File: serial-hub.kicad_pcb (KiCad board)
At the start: 2 copper layers, 100 x 100 mm, 55 parts, among them J1 USB_C_Receptacle_USB2.0, J2 RJ45_LED_Shielded, J3 RJ45_LED_Shielded, J4 RJ45_LED_Shielded, J5 RJ45_LED_Shielded, U1 CH344, U2 AMS1117-3.3, U3 MAX232, U4 MAX232, U5 MAX232, U6 MAX232, Y1 8MHz

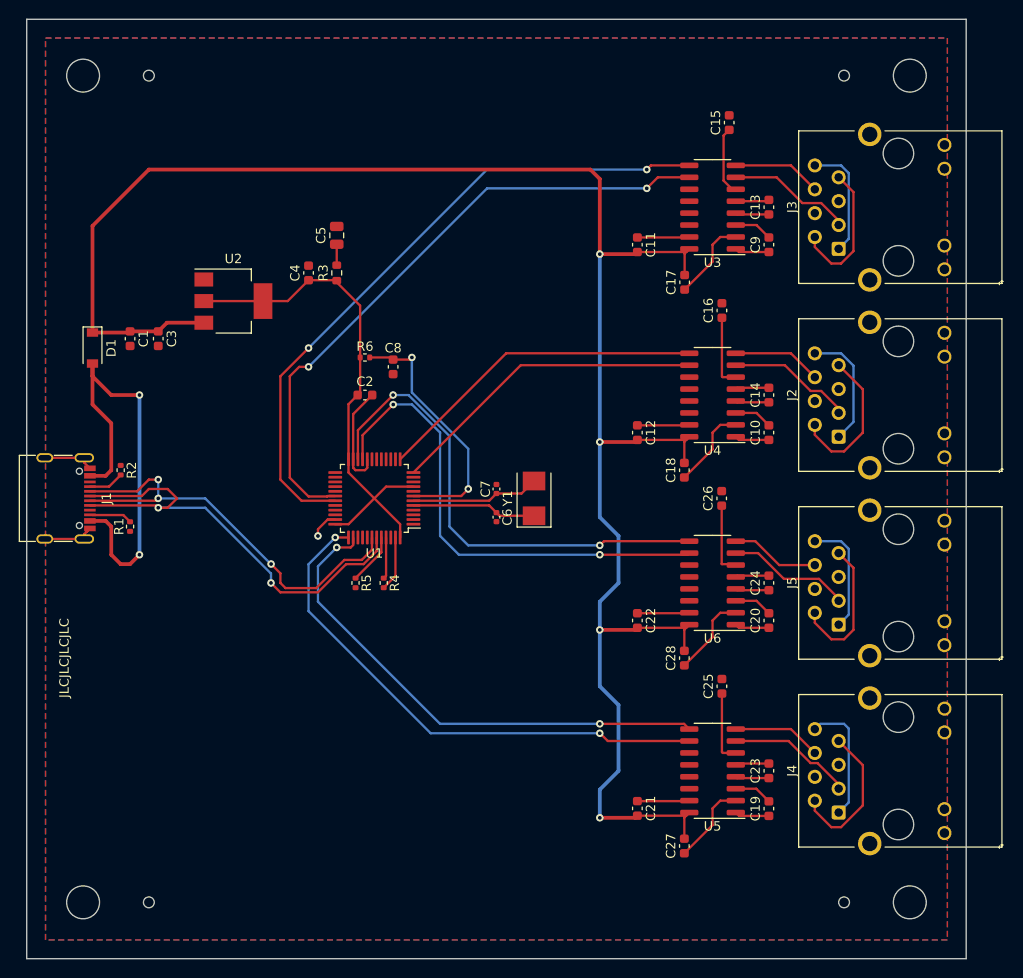
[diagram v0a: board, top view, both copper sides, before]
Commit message: add test-pins for UART
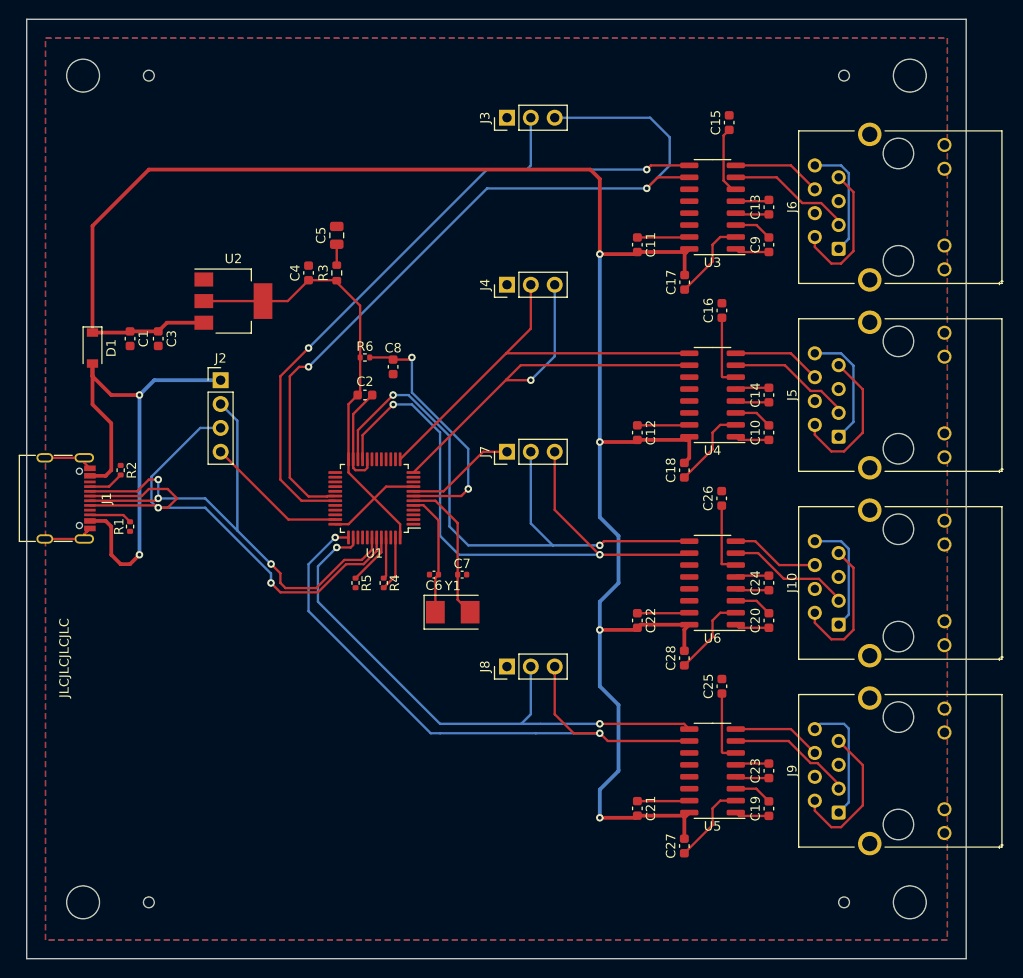
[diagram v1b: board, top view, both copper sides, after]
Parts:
- added J2: Conn_01x04_Male, Connector_PinHeader_2.54mm:PinHeader_1x04_P2.54mm_Vertical, F.Cu at (40.6, 58.4)
- added J3: Conn_01x03_Male, Connector_PinHeader_2.54mm:PinHeader_1x03_P2.54mm_Vertical, F.Cu at (71.1, 30.5)
- added J4: Conn_01x03_Male, Connector_PinHeader_2.54mm:PinHeader_1x03_P2.54mm_Vertical, F.Cu at (71.1, 48.3)
- added J7: Conn_01x03_Male, Connector_PinHeader_2.54mm:PinHeader_1x03_P2.54mm_Vertical, F.Cu at (71.1, 66.0)
- added J8: Conn_01x03_Male, Connector_PinHeader_2.54mm:PinHeader_1x03_P2.54mm_Vertical, F.Cu at (71.1, 88.9)
- moved Y1 14.9 mm to (65.3, 83.1), turned to 0 degrees
- moved C7 9.82 mm to (66.3, 79.1), turned to 0 degrees
- moved C6 9.03 mm to (63.4, 79.1), turned to 180 degrees
- renumbered J5 to J10, J2 to J5, J3 to J6, J4 to J9
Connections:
- net Net-(D1-Pad2) renamed VCC
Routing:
- net GND: track 53.9 -> 77.8 mm, vias 1 -> 0
- net /C0_TX: track 67.8 -> 87.3 mm
- net /HOST_DM: track 47.5 -> 61.7 mm
- net /C1_TX: track 34.1 -> 47.9 mm, vias 0 -> 1
- net /HOST_DP: track 50.6 -> 63.8 mm
- net /C2_TX: track 51.8 -> 64.8 mm
- net /C2_RX: track 52.4 -> 63.3 mm
- net /C3_TX: track 56.7 -> 67.4 mm
- net VCC: track 48.2 -> 57.5 mm
- net /C1_RX: track 35.4 -> 43.8 mm
- net /C3_RX: track 54.4 -> 60.9 mm
- net /C0_RX: track 70.6 -> 76.3 mm
- net /CH344_XO: track 13.7 -> 15.7 mm

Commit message: switch USB-C / add CH344 input caps
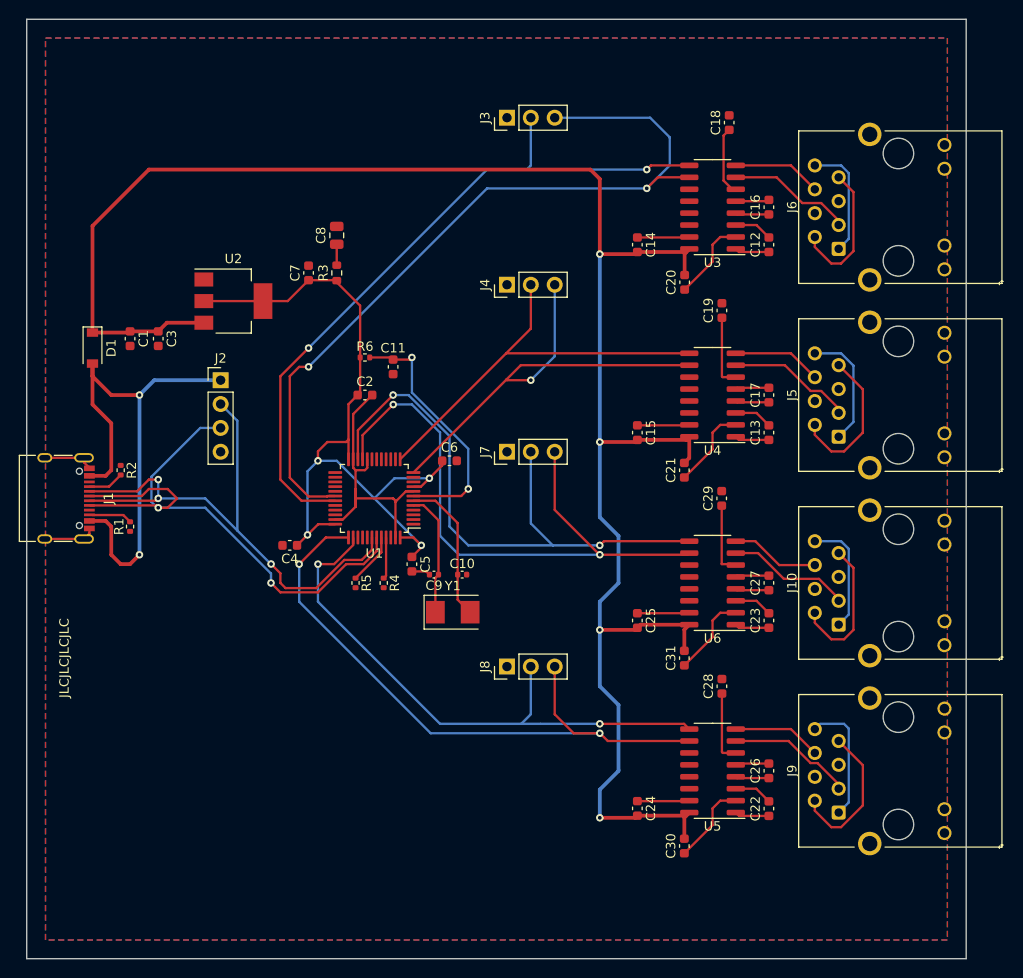
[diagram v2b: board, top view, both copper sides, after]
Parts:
- removed REF** (x4): MountingHole_2.1mm, MountingHole:MountingHole_2.1mm
- removed REF** (x4): MountingHole_3.5mm, MountingHole:MountingHole_3.5mm
- added C4: 0.1uF, Capacitor_SMD:C_0603_1608Metric, F.Cu at (48.0, 76.0)
- added C5: 0.1uF, Capacitor_SMD:C_0603_1608Metric, F.Cu at (61.0, 78.0)
- added C6: 0.1uF, Capacitor_SMD:C_0603_1608Metric, F.Cu at (65.0, 67.0)
- J1: footprint Connector_USB:USB_C_Receptacle_G-Switch_GT-USB-7010ASV -> Connector_USB:USB_C_Receptacle_XKB_U262-16XN-4BVC11
- renumbered C7 to C10, C8 to C11, C9 to C12, C10 to C13, C11 to C14, C12 to C15, C13 to C16, C14 to C17, C15 to C18, C16 to C19, C17 to C20, C18 to C21, C19 to C22, C20 to C23, C21 to C24, C22 to C25, C23 to C26, C24 to C27, C25 to C28, C26 to C29, C27 to C30, C28 to C31, C4 to C7, C5 to C8, C6 to C9
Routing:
- net +3.3V: track 56.2 -> 83.9 mm, vias 0 -> 4
- net GND: track 77.8 -> 66.1 mm
- net /C3_TX: track 67.4 -> 68.8 mm
- net VCC: track 57.5 -> 58.1 mm

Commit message: add mounting holes
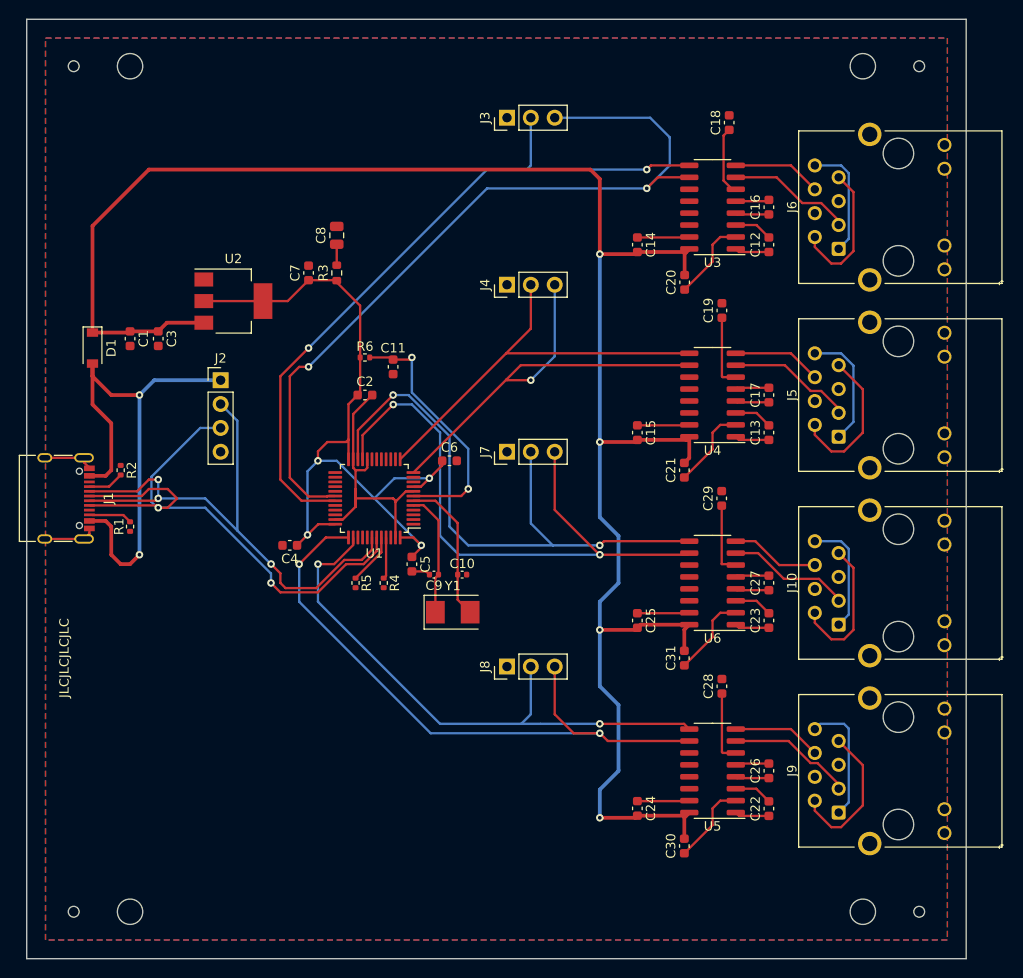
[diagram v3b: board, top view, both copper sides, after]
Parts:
- added REF**: MountingHole_2.7mm_M2.5, MountingHole:MountingHole_2.7mm_M2.5, F.Cu at (31.0, 115.0)
- added REF**: MountingHole_2.1mm, MountingHole:MountingHole_2.1mm, F.Cu at (115.0, 25.0)
- added REF**: MountingHole_2.7mm_M2.5, MountingHole:MountingHole_2.7mm_M2.5, F.Cu at (109.0, 115.0)
- added REF**: MountingHole_2.7mm_M2.5, MountingHole:MountingHole_2.7mm_M2.5, F.Cu at (109.0, 25.0)
- added REF**: MountingHole_2.1mm, MountingHole:MountingHole_2.1mm, F.Cu at (25.0, 115.0)
- added REF**: MountingHole_2.1mm, MountingHole:MountingHole_2.1mm, F.Cu at (25.0, 25.0)
- added REF**: MountingHole_2.1mm, MountingHole:MountingHole_2.1mm, F.Cu at (115.0, 115.0)
- added REF**: MountingHole_2.7mm_M2.5, MountingHole:MountingHole_2.7mm_M2.5, F.Cu at (31.0, 25.0)
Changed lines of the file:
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@@
     )
+  )
+  (footprint "MountingHole:MountingHole_2.7mm_M2.5" (layer "F.Cu")
+    (at 31 115)
+    (descr "Mounting Hole 2.7mm, no annular, M2.5")
+    (tags "mounting hole 2.7mm no annular m2.5")
+    (attr exclude_from_pos_files exclude_from_bom)
+    (fp_text reference "REF**" (at 0 -3.7) (layer "F.SilkS") hide
+      (effects (font (size 1 1) (thickness 0.15)))
+    )
+    (fp_text value "MountingHole_2.7mm_M2.5" (at 0 3.7) (layer "F.Fab")
+      (effects (font (size 1 1) (thickness 0.15)))
+    )
+    (fp_text user "${REFERENCE}" (at 0 0) (layer "F.Fab")
+      (effects (font (size 1 1) (thickness 0.15)))
+    )
+    (fp_circle (center 0 0) (end 2.7 0) (layer "Cmts.User") (width 0.15) (fill none))
+    (fp_circle (center 0 0) (end 2.95 0) (layer "F.CrtYd") (width 0.05) (fill none))
+    (pad "" np_thru_hole circle (at 0 0) (size 2.7 2.7) (drill 2.7) (layers F&B.Cu *.Mask))
   )
   (footprint "Capacitor_SMD:C_0603_1608Metric" (layer "F.Cu")
@@
     )
   )
+  (footprint "MountingHole:MountingHole_2.1mm" (layer "F.Cu")
+    (at 115 25)
+    (descr "Mounting Hole 2.1mm, no annular")
+    (tags "mounting hole 2.1mm no annular")
+    (attr exclude_from_pos_files exclude_from_bom)
+    (fp_text reference "REF**" (at 0 -3.2) (layer "F.SilkS") hide
+      (effects (font (size 1 1) (thickness 0.15)))
+    )
+    (fp_text value "MountingHole_2.1mm" (at 0 3.2) (layer "F.Fab")
+      (effects (font (size 1 1) (thickness 0.15)))
+    )
+    (fp_text user "${REFERENCE}" (at 0 0) (layer "F.Fab")
+      (effects (font (size 1 1) (thickness 0.15)))
+    )
+    (fp_circle (center 0 0) (end 2.1 0) (layer "Cmts.User") (width 0.15) (fill none))
+    (fp_circle (center 0 0) (end 2.35 0) (layer "F.CrtYd") (width 0.05) (fill none))
+    (pad "" np_thru_hole circle (at 0 0) (size 1.152 1.152) (drill 1.152) (layers F&B.Cu *.Mask))
+  )
   (footprint "Capacitor_SMD:C_0603_1608Metric" (layer "F.Cu")
     (at 59 57 -90)
@@
       (rotate (xyz 0 0 0))
     )
+  )
+  (footprint "MountingHole:MountingHole_2.7mm_M2.5" (layer "F.Cu")
+    (at 109 115)
+    (descr "Mounting Hole 2.7mm, no annular, M2.5")
+    (tags "mounting hole 2.7mm no annular m2.5")
+    (attr exclude_from_pos_files exclude_from_bom)
+    (fp_text reference "REF**" (at 0 -3.7) (layer "F.SilkS") hide
+      (effects (font (size 1 1) (thickness 0.15)))
+    )
+    (fp_text value "MountingHole_2.7mm_M2.5" (at 0 3.7) (layer "F.Fab")
+      (effects (font (size 1 1) (thickness 0.15)))
+    )
+    (fp_text user "${REFERENCE}" (at 0 0) (layer "F.Fab")
+      (effects (font (size 1 1) (thickness 0.15)))
+    )
+    (fp_circle (center 0 0) (end 2.7 0) (layer "Cmts.User") (width 0.15) (fill none))
+    (fp_circle (center 0 0) (end 2.95 0) (layer "F.CrtYd") (width 0.05) (fill none))
+    (pad "" np_thru_hole circle (at 0 0) (size 2.7 2.7) (drill 2.7) (layers F&B.Cu *.Mask))
   )
   (footprint "Connector_PinHeader_2.54mm:PinHeader_1x03_P2.54mm_Vertical" (layer "F.Cu")
@@
     )
   )
+  (footprint "MountingHole:MountingHole_2.7mm_M2.5" (layer "F.Cu")
+    (at 109 25)
+    (descr "Mounting Hole 2.7mm, no annular, M2.5")
+    (tags "mounting hole 2.7mm no annular m2.5")
+    (attr exclude_from_pos_files exclude_from_bom)
+    (fp_text reference "REF**" (at 0 -3.7) (layer "F.SilkS") hide
+      (effects (font (size 1 1) (thickness 0.15)))
+    )
+    (fp_text value "MountingHole_2.7mm_M2.5" (at 0 3.7) (layer "F.Fab")
+      (effects (font (size 1 1) (thickness 0.15)))
+    )
+    (fp_text user "${REFERENCE}" (at 0 0) (layer "F.Fab")
+      (effects (font (size 1 1) (thickness 0.15)))
+    )
+    (fp_circle (center 0 0) (end 2.7 0) (layer "Cmts.User") (width 0.15) (fill none))
+    (fp_circle (center 0 0) (end 2.95 0) (layer "F.CrtYd") (width 0.05) (fill none))
+    (pad "" np_thru_hole circle (at 0 0) (size 2.7 2.7) (drill 2.7) (layers F&B.Cu *.Mask))
+  )
   (footprint "Package_SO:SOIC-16_3.9x9.9mm_P1.27mm" (layer "F.Cu")
     (at 93 40 180)
@@
     )
   )
+  (footprint "MountingHole:MountingHole_2.1mm" (layer "F.Cu")
+    (at 25 115)
+    (descr "Mounting Hole 2.1mm, no annular")
+    (tags "mounting hole 2.1mm no annular")
+    (attr exclude_from_pos_files exclude_from_bom)
+    (fp_text reference "REF**" (at 0 -3.2) (layer "F.SilkS") hide
+      (effects (font (size 1 1) (thickness 0.15)))
+    )
+    (fp_text value "MountingHole_2.1mm" (at 0 3.2) (layer "F.Fab")
+      (effects (font (size 1 1) (thickness 0.15)))
+    )
+    (fp_text user "${REFERENCE}" (at 0 0) (layer "F.Fab")
+      (effects (font (size 1 1) (thickness 0.15)))
+    )
+    (fp_circle (center 0 0) (end 2.1 0) (layer "Cmts.User") (width 0.15) (fill none))
+    (fp_circle (center 0 0) (end 2.35 0) (layer "F.CrtYd") (width 0.05) (fill none))
+    (pad "" np_thru_hole circle (at 0 0) (size 1.152 1.152) (drill 1.152) (layers F&B.Cu *.Mask))
+  )
   (footprint "Capacitor_SMD:C_0603_1608Metric" (layer "F.Cu")
     (at 99 100 90)
@@
       (rotate (xyz 0 0 0))
     )
+  )
+  (footprint "MountingHole:MountingHole_2.1mm" (layer "F.Cu")
+    (at 25 25)
+    (descr "Mounting Hole 2.1mm, no annular")
+    (tags "mounting hole 2.1mm no annular")
+    (attr exclude_from_pos_files exclude_from_bom)
+    (fp_text reference "REF**" (at 0 -3.2) (layer "F.SilkS") hide
+      (effects (font (size 1 1) (thickness 0.15)))
+    )
+    (fp_text value "MountingHole_2.1mm" (at 0 3.2) (layer "F.Fab")
+      (effects (font (size 1 1) (thickness 0.15)))
+    )
+    (fp_text user "${REFERENCE}" (at 0 0) (layer "F.Fab")
+      (effects (font (size 1 1) (thickness 0.15)))
+    )
+    (fp_circle (center 0 0) (end 2.1 0) (layer "Cmts.User") (width 0.15) (fill none))
+    (fp_circle (center 0 0) (end 2.35 0) (layer "F.CrtYd") (width 0.05) (fill none))
+    (pad "" np_thru_hole circle (at 0 0) (size 1.152 1.152) (drill 1.152) (layers F&B.Cu *.Mask))
   )
   (footprint "Capacitor_SMD:C_0603_1608Metric" (layer "F.Cu")
@@
       (rotate (xyz 0 0 0))
     )
+  )
+  (footprint "MountingHole:MountingHole_2.1mm" (layer "F.Cu")
+    (at 115 115)
+    (descr "Mounting Hole 2.1mm, no annular")
+    (tags "mounting hole 2.1mm no annular")
+    (attr exclude_from_pos_files exclude_from_bom)
+    (fp_text reference "REF**" (at 0 -3.2) (layer "F.SilkS") hide
+      (effects (font (size 1 1) (thickness 0.15)))
+    )
+    (fp_text value "MountingHole_2.1mm" (at 0 3.2) (layer "F.Fab")
+      (effects (font (size 1 1) (thickness 0.15)))
+    )
+    (fp_text user "${REFERENCE}" (at 0 0) (layer "F.Fab")
+      (effects (font (size 1 1) (thickness 0.15)))
+    )
+    (fp_circle (center 0 0) (end 2.1 0) (layer "Cmts.User") (width 0.15) (fill none))
+    (fp_circle (center 0 0) (end 2.35 0) (layer "F.CrtYd") (width 0.05) (fill none))
+    (pad "" np_thru_hole circle (at 0 0) (size 1.152 1.152) (drill 1.152) (layers F&B.Cu *.Mask))
   )
   (footprint "Connector_RJ:RJ45_Hanrun_HR911105A" (layer "F.Cu")
@@
     )
   )
+  (footprint "MountingHole:MountingHole_2.7mm_M2.5" (layer "F.Cu")
+    (at 31 25)
+    (descr "Mounting Hole 2.7mm, no annular, M2.5")
+    (tags "mounting hole 2.7mm no annular m2.5")
+    (attr exclude_from_pos_files exclude_from_bom)
+    (fp_text reference "REF**" (at 0 -3.7) (layer "F.SilkS") hide
+      (effects (font (size 1 1) (thickness 0.15)))
+    )
+    (fp_text value "MountingHole_2.7mm_M2.5" (at 0 3.7) (layer "F.Fab")
+      (effects (font (size 1 1) (thickness 0.15)))
+    )
+    (fp_text user "${REFERENCE}" (at 0 0) (layer "F.Fab")
+      (effects (font (size 1 1) (thickness 0.15)))
+    )
+    (fp_circle (center 0 0) (end 2.7 0) (layer "Cmts.User") (width 0.15) (fill none))
+    (fp_circle (center 0 0) (end 2.95 0) (layer "F.CrtYd") (width 0.05) (fill none))
+    (pad "" np_thru_hole circle (at 0 0) (size 2.7 2.7) (drill 2.7) (layers *.Cu *.Mask))
+  )
   (footprint "Connector_RJ:RJ45_Hanrun_HR911105A" (layer "F.Cu")
